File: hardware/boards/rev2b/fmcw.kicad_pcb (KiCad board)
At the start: 4 copper layers, 118.6 x 62 mm, 445 parts, among them CON1 BARREL_JACK, J1 SD_Card, J2 USB_B_Micro, J3 SMA, J4 SMA, J5 SMA, J6 Conn_02x08_Odd_Even, Q1 DNP(RE1C002UN), Q2 RE1C002UN, SW1 SW_PUSH, T1 uwave, T10 uwave, T11 uwave, T12 uwave, T13 uwave, T14 uwave, T15 uwave, T16 uwave, T2 uwave, T3 uwave, T4 uwave, T5 uwave, T6 uwave, T7 uwave, T8 uwave, T9 uwave, U1 LP5907MFX-3.3, U10 LP5907MFX-3.0, U11 LTC2292, U12 ADF4158, U13 TLV172DCK, U14 PS2012GT2-R50, U15 HMC431, U17 PAT1220-C-2DB, U18 SE5004L, U2 LP5907MFX-1.8, U20 PAT1220-C-6DB, U21 LMV321, U22 TRF37A73, U23 SKY65404, U24 TRF37A73, U25 SKY65404, U26 L7980, U27 L7980, U28 L7980, U29 LP2985A-10DBVR, U3 KT2520K-T, U30 TPS7A91, U31 TPS7A91, U32 TPS7A91, U33 LP5907MFX-3.0, U34 TPS7A91, U35 5400BL15B050E, U36 5400BL15B050E, U37 5400BL15B050E, U38 ADL5802, U39 ADA4940-2, U4 NC7SVU04P5X, U40 TPS7A91, U5 NB3N551, U6 XC7A15T-FTG256, U7 MX25L3233F, U8 93LCxxBxxOT, U9 FT2232H, Y1 12MHz

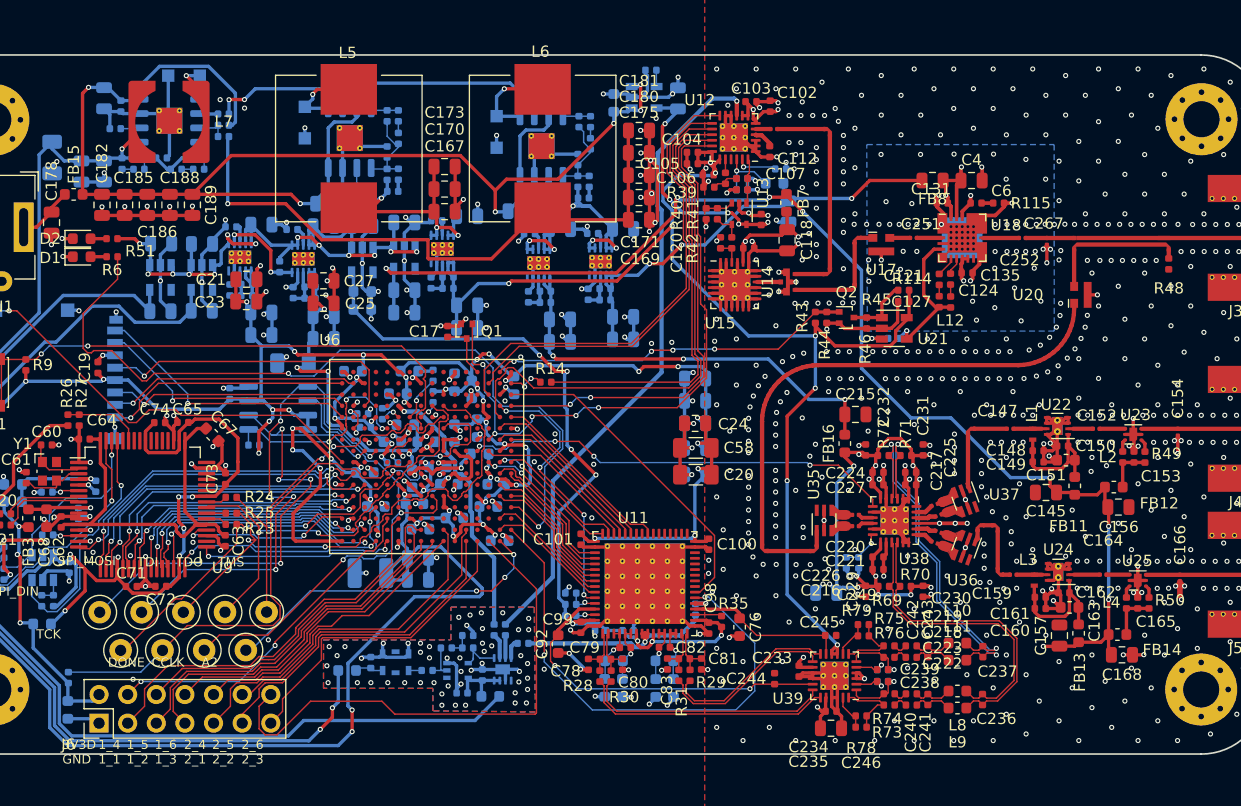
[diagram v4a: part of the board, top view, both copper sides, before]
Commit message: rev2b: add return path vias
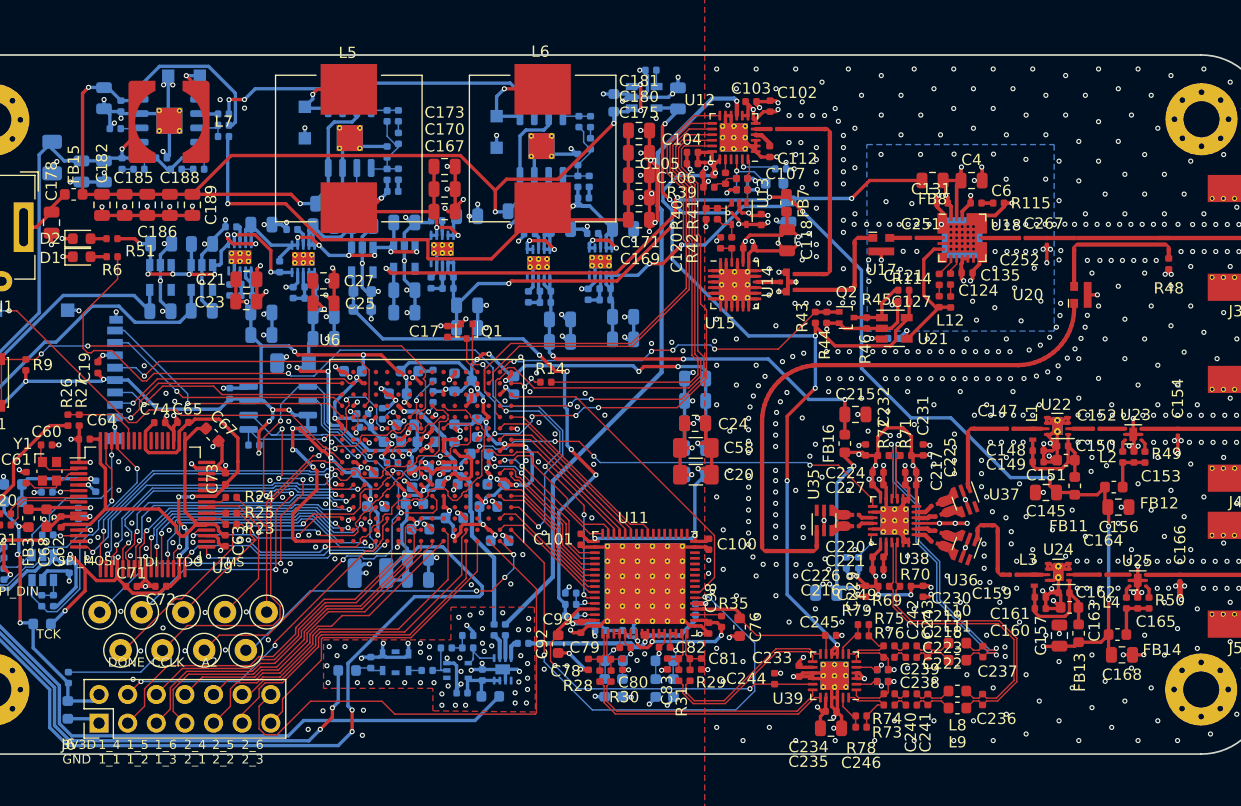
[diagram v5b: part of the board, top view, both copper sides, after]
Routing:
- net GND: track 596.7 -> 628.9 mm, vias 801 -> 901
- net /mixer/5VF: track 51.6 -> 53.7 mm
- net /fpga/usb/1V8: track 38.5 -> 36.7 mm
- net /fpga/usb/EEDATA: track 22.1 -> 23.3 mm
- net /fpga/SPI_DIN: track 47.0 -> 45.9 mm
- net /fpga/D4: track 11.8 -> 12.7 mm
- net /fpga/SD_DAT0: track 23.2 -> 22.5 mm
- net /fpga/FT_D4: track 24.9 -> 25.6 mm
- net Net-(R12-Pad2): track 46.2 -> 46.8 mm
- net /fpga/SPI_MOSI: track 44.9 -> 45.5 mm
- net /fpga/SD_CMD: track 21.0 -> 21.6 mm
